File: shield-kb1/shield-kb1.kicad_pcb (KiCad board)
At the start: 2 copper layers, 65.5 x 53 mm, 13 parts, among them J1 LEFT, J2 RIGHT, SW1 SW_SPST, SW2 SW_SPST, SW3 SW_SPST, SW4 SW_SPST

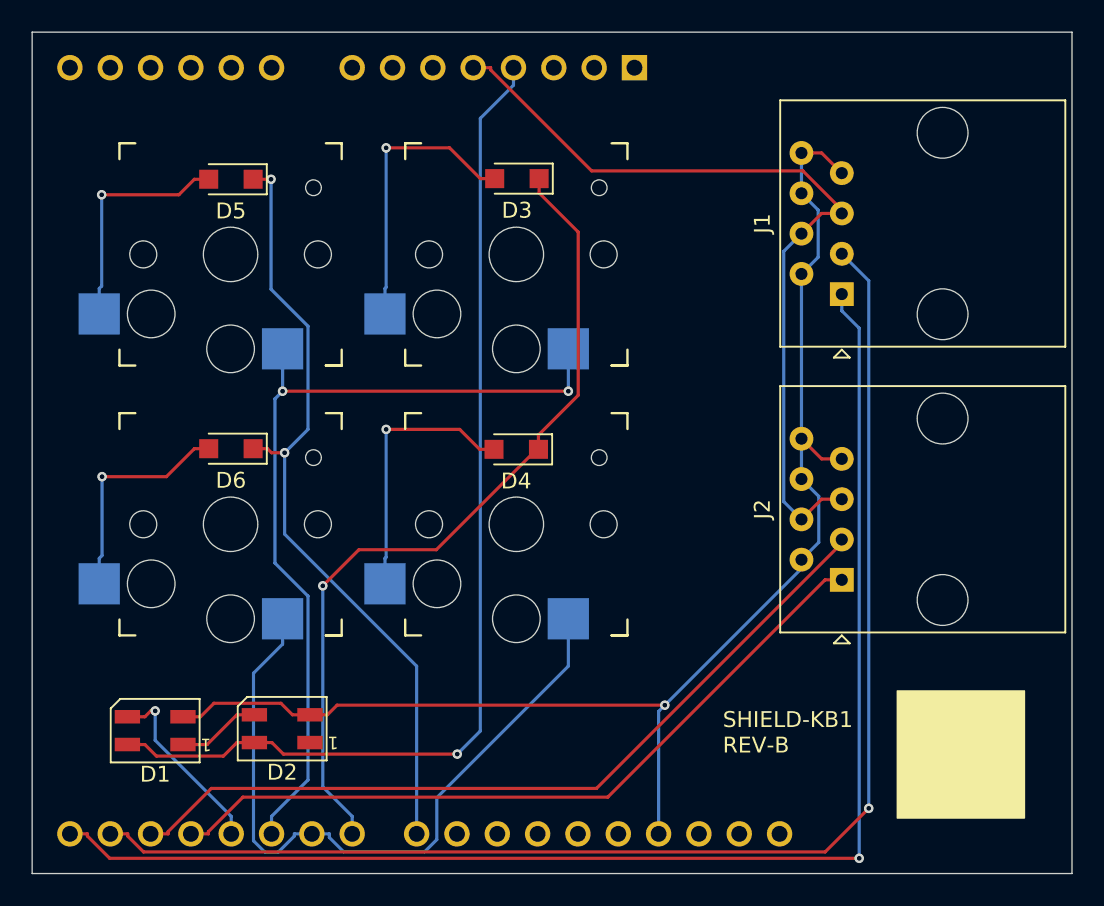
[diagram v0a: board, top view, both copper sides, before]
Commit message: shield-kb1: rev-b updates: LEDs
In addition to actually hooking up the switches, add a PWM RGB LED. It
is hard to find these that will work with 3.2V, hopefully this one will.
It is fairly small, and I've come up with some resistors for about 15mA.

I've also added a jumper to allow the SK6812 to be powered either from
3.3V or 5V, which should help figring out issues with that.
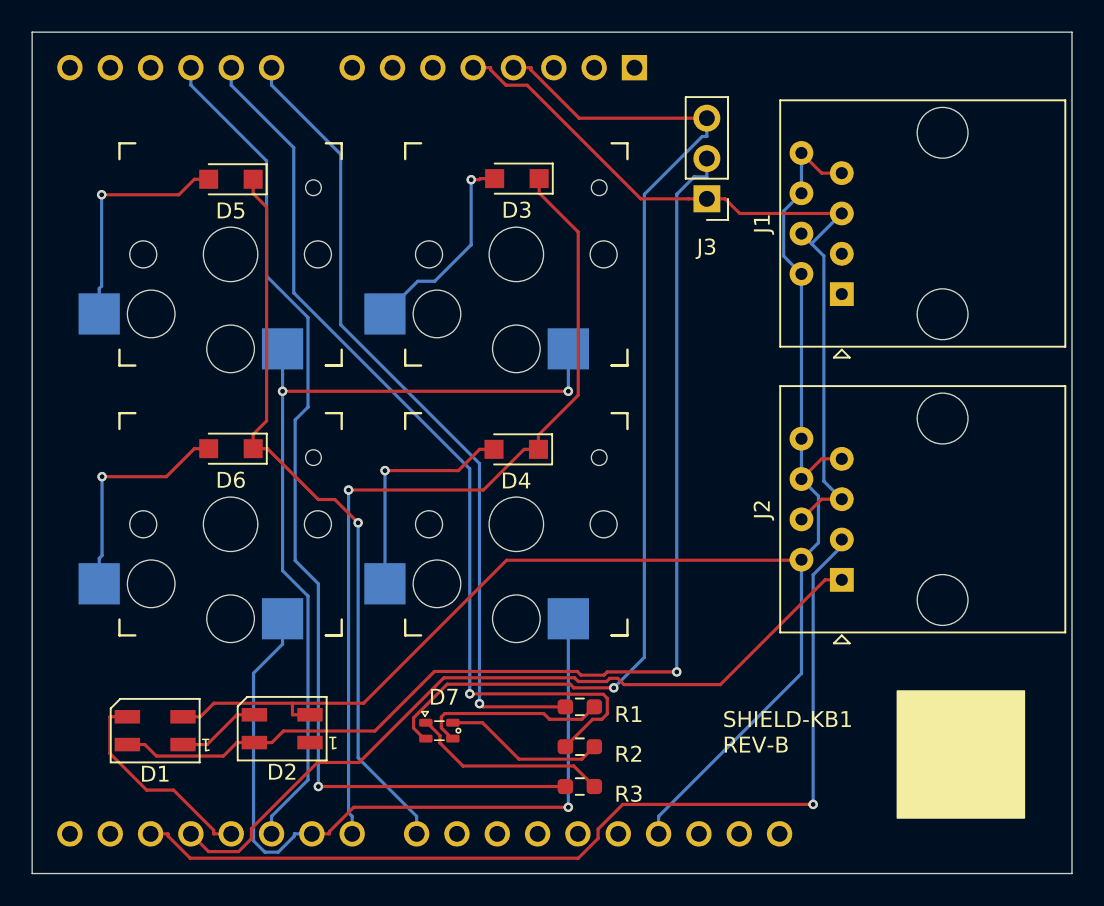
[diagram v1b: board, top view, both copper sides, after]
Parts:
- added D7: QBLP600-RGB5-2897, davidb-keyboard-foot:QBLP600-RGB5-2897, F.Cu at (67.2, 123.5)
- added J3: Conn_01x03_Pin, Connector_PinHeader_2.54mm:PinHeader_1x03_P2.54mm_Vertical, F.Cu at (84.0, 90.0)
- added R1: 100, Resistor_SMD:R_0603_1608Metric_Pad0.98x0.95mm_HandSolder, F.Cu at (76.0, 122.0)
- added R2: 33, Resistor_SMD:R_0603_1608Metric_Pad0.98x0.95mm_HandSolder, F.Cu at (76.0, 124.5)
- added R3: 33, Resistor_SMD:R_0603_1608Metric_Pad0.98x0.95mm_HandSolder, F.Cu at (76.0, 127.0)
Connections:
- A1 pad 10: unconnected-(A1-A1-Pad10) -> /LED-G
- A1 pad 11: unconnected-(A1-A2-Pad11) -> /LED-B
- A1 pad 9: unconnected-(A1-A0-Pad9) -> /LED-R
- D1 pad 4: +3.3V -> Net-(D1-VDD)
- D2 pad 4: +3.3V -> Net-(D1-VDD)
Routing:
- net /LEFT-RX: track 86.4 -> 0.00 mm, vias 1 -> 0
- net /LEFT-TX: track 85.1 -> 0.00 mm, vias 1 -> 0
- net Net-(D1-VDD): track 0.00 -> 70.9 mm, vias 0 -> 1
- net /LED-B: track 0.00 -> 64.8 mm, vias 0 -> 1
- net /LED-G: track 0.00 -> 58.9 mm, vias 0 -> 1
- net /LED-R: track 0.00 -> 51.0 mm, vias 0 -> 1
- net GND: track 85.8 -> 99.5 mm, vias 1 -> 0
- net Net-(D7-BK): track 0.00 -> 12.6 mm
- net Net-(D7-RK): track 0.00 -> 11.9 mm
- net /RIGHT-RX: track 51.4 -> 61.6 mm, vias 0 -> 1
- net Net-(D7-GK): track 0.00 -> 10.2 mm
- net Net-(D3-A): track 18.1 -> 12.8 mm
- net /COL-B: track 45.4 -> 48.1 mm, vias 0 -> 1
- net Net-(D4-A): track 17.1 -> 14.6 mm
- net /ROW-B: track 49.5 -> 47.3 mm, vias 2 -> 1
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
